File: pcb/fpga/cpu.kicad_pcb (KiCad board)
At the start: 2 copper layers, 0 parts

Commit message: Latest pcb
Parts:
- added C1: 10uF, Capacitors_SMD:C_0805_HandSoldering, F.Cu at (212.1, 82.5)
- added C10: 0.2uF, Capacitors_SMD:C_0805_HandSoldering, B.Cu at (240.0, 83.8)
- added C11: 0.2uF, Capacitors_SMD:C_0805_HandSoldering, B.Cu at (240.0, 88.9)
- added C12: 0.2uF, Capacitors_SMD:C_0805_HandSoldering, B.Cu at (240.0, 94.0)
- added C13: 0.2uF, Capacitors_SMD:C_0805_HandSoldering, B.Cu at (248.9, 78.7)
- added C14: 0.2uF, Capacitors_SMD:C_0805_HandSoldering, B.Cu at (248.9, 83.8)
- added C15: 0.2uF, Capacitors_SMD:C_0805_HandSoldering, B.Cu at (248.9, 88.9)
- added C16: 0.2uF, Capacitors_SMD:C_0805_HandSoldering, B.Cu at (248.9, 94.0)
- added C17: 0.2uF, Capacitors_SMD:C_0805_HandSoldering, B.Cu at (248.9, 99.1)
- added C18: 0.2uF, Capacitors_SMD:C_0805_HandSoldering, B.Cu at (248.9, 104.1)
- added C19: 10uF, Capacitors_SMD:c_elec_4x5.3, F.Cu at (188.0, 94.0)
- added C2: 100uF, Capacitors_SMD:C_0805_HandSoldering, B.Cu at (240.0, 68.6)
- added C20: 1000uF, Capacitors_SMD:c_elec_4x5.3, F.Cu at (198.1, 94.0)
- added C21: 10uF, Capacitors_SMD:c_elec_4x5.3, F.Cu at (204.5, 88.9)
- added C22: 10uF, Capacitors_SMD:c_elec_4x5.3, F.Cu at (218.4, 80.0)
- added C23: 0.1uF, Capacitors_SMD:C_0805, B.Cu at (228.6, 68.6)
- added C24: 0.001uF, Capacitors_SMD:C_0805, B.Cu at (223.5, 68.6)
- added C25: 10uF, Capacitors_SMD:C_0805, F.Cu at (247.7, 81.3)
- added C3: 0.01uF, Capacitors_SMD:C_0805_HandSoldering, B.Cu at (240.0, 73.7)
- added C4: 100uF, Capacitors_SMD:C_0805_HandSoldering, B.Cu at (248.9, 68.6)
- added C5: 0.01uF, Capacitors_SMD:C_0805_HandSoldering, B.Cu at (248.9, 73.7)
- added C6: 10uF, Capacitors_SMD:c_elec_4x4.5, F.Cu at (188.0, 73.7)
- added C7: 1000uF, Capacitors_SMD:c_elec_4x4.5, F.Cu at (198.1, 73.7)
- added C8: 10uF, Capacitors_SMD:c_elec_4x4.5, F.Cu at (204.5, 80.0)
- added C9: 0.2uF, Capacitors_SMD:C_0805_HandSoldering, B.Cu at (240.0, 78.7)
- added CON1: USB-MINI-B, Connect:USB_Mini-B, F.Cu at (188.0, 83.8)
- added D1: LED, LEDs:LED-0805, F.Cu at (222.9, 59.1)
- added D2: LED, LEDs:LED-0805, F.Cu at (219.1, 59.1)
- added D3: LED, LEDs:LED-0805, F.Cu at (215.3, 59.1)
- added D4: LED, LEDs:LED-0805, F.Cu at (211.5, 59.1)
- added D5: LED, LEDs:LED-0805, F.Cu at (207.6, 59.1)
- added D6: LED, LEDs:LED-0805, F.Cu at (203.8, 59.1)
- added D7: LED, LEDs:LED-0805, F.Cu at (200.0, 59.1)
- added D8: LED, LEDs:LED-0805, F.Cu at (196.2, 59.1)
- added FB1: FILTER, Resistors_SMD:R_0805_HandSoldering, F.Cu at (198.1, 83.8)
- added FB2: FILTER, Resistors_SMD:R_0805_HandSoldering, B.Cu at (233.7, 68.6)
- added OSC1: Si501AAA, common-ICs:DFN4-Si501, F.Cu at (223.5, 88.9)
- added P1: PWR, Pin_Headers:Pin_Header_Straight_1x02, F.Cu at (256.5, 101.6)
- added P2: BANK3, Pin_Headers:Pin_Header_Straight_2x08, F.Cu at (254.0, 58.4)
- added P3: BANK1, Pin_Headers:Pin_Header_Straight_2x06, F.Cu at (205.7, 104.1)
- added P4: BANK2, Pin_Headers:Pin_Header_Straight_2x09, F.Cu at (248.9, 58.4)
- added P5: BANK4, Pin_Headers:Pin_Header_Straight_2x09, F.Cu at (243.8, 101.6)
- added P6: CONN_6, Pin_Headers:Pin_Header_Straight_1x06, F.Cu at (256.5, 82.5)
- added R1: 10M, Resistors_SMD:R_0805_HandSoldering, F.Cu at (247.7, 88.9)
- added R2: 24.9, Resistors_SMD:R_0805_HandSoldering, F.Cu at (224.8, 81.3)
- added RP1: 10K, Resistors_SMD:R_Array_Convex_4x1206, F.Cu at (215.9, 95.2)
- added RP2: 270, Housings_DIP:DIP-16_W7.62mm, F.Cu at (222.2, 64.8)
- added U1: EPCS1, SMD_Packages:SOIC-8-N, F.Cu at (213.4, 87.6)
- added U2: LMS1585/7, SMD_Packages:TO-263, B.Cu at (193.0, 76.2)
- added U3: LM1084IS-3.3/NOPB, SMD_Packages:TO-263, B.Cu at (193.0, 91.4)
- added U4: EP1C3T100, Housings_QFP:TQFP-100_14x14mm_Pitch0.5mm, F.Cu at (236.2, 81.3)
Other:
- board outline added: 76.2 x 50.8 mm
- net class Default: clearance 0.254 -> 0.1524; trace_width 0.254 -> 0.1524; via_dia 0.889 -> 0.635; via_drill 0.635 -> 0.3302
- rule trace_clearance: 0.254 -> 0.1524
- rule trace_min: 0.254 -> 0.1524
- rule via_min_drill: 0.508 -> 0.3302
- rule via_min_size: 0.889 -> 0.635

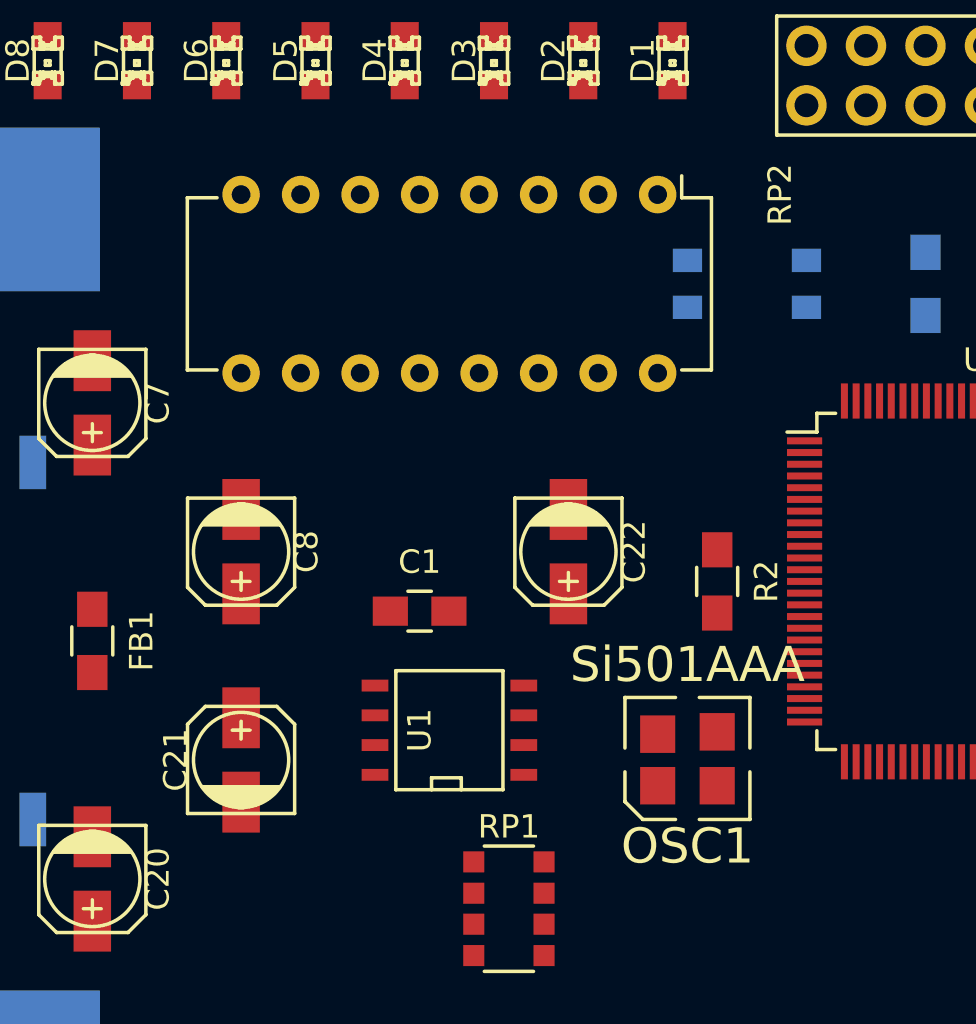
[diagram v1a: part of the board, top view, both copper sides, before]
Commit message: Resistors replacing resistor network
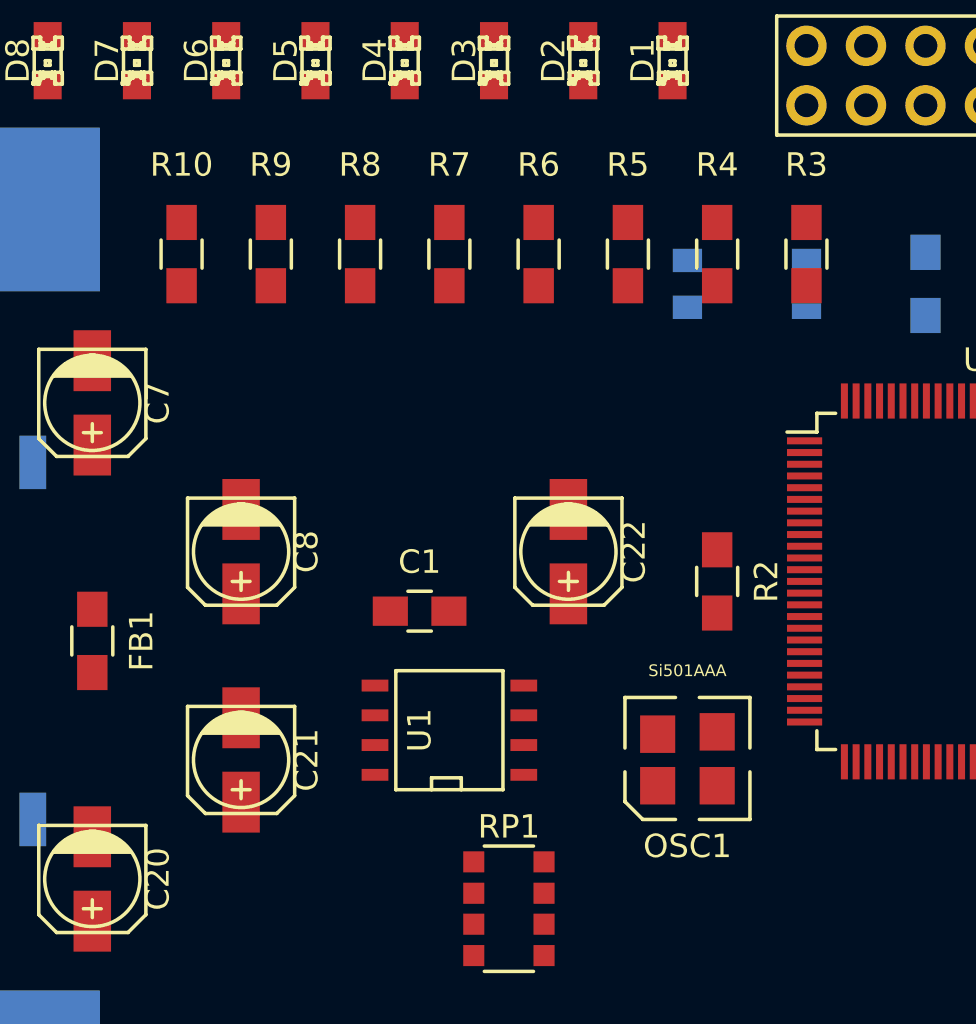
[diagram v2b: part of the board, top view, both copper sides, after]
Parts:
- removed RP2: 270, Housings_DIP:DIP-16_W7.62mm
- added R10: 270, Resistors_SMD:R_0805_HandSoldering, F.Cu at (201.9, 67.3)
- added R3: 270, Resistors_SMD:R_0805_HandSoldering, F.Cu at (228.6, 67.3)
- added R4: 270, Resistors_SMD:R_0805_HandSoldering, F.Cu at (224.8, 67.3)
- added R5: 270, Resistors_SMD:R_0805_HandSoldering, F.Cu at (221.0, 67.3)
- added R6: 270, Resistors_SMD:R_0805_HandSoldering, F.Cu at (217.2, 67.3)
- added R7: 270, Resistors_SMD:R_0805_HandSoldering, F.Cu at (213.4, 67.3)
- added R8: 270, Resistors_SMD:R_0805_HandSoldering, F.Cu at (209.6, 67.3)
- added R9: 270, Resistors_SMD:R_0805_HandSoldering, F.Cu at (205.7, 67.3)
- turned C21 to 270 degrees
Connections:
- net +1.5V renamed VCCINT

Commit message: Layout changes
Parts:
- moved P4 20.5 mm to (228.6, 61.0), turned to 90 degrees
- moved P3 13.0 mm to (218.4, 101.6), turned to 270 degrees
- moved C20 1.27 mm to (196.8, 94.0)
- moved C7 1.27 mm to (196.8, 73.7)
- moved C19 1.27 mm to (189.2, 94.0)
- moved C6 1.27 mm to (189.2, 73.7)
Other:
- board text added: "JTAG"

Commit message: Layout changes
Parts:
- moved R4 1.27 mm to (224.8, 68.6)
- moved R10 0.32 mm to (201.9, 67.6)
- moved R6 0.32 mm to (217.2, 67.6)
- moved R7 0.32 mm to (213.4, 67.6)
- moved R8 0.32 mm to (209.6, 67.6)
- moved R9 0.32 mm to (205.7, 67.6)
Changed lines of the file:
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@@
   )
   (module Resistors_SMD:R_0805_HandSoldering (layer F.Cu)
-    (at 224.79 67.31 90)
+    (at 224.79 68.58 90)
     (descr "Resistor SMD 0805, hand soldering")
     (tags "resistor 0805")
@@
   )
   (module Resistors_SMD:R_0805_HandSoldering (layer F.Cu)
-    (at 217.17 67.31 90)
+    (at 217.17 67.63 90)
     (descr "Resistor SMD 0805, hand soldering")
     (tags "resistor 0805")
@@
   )
   (module Resistors_SMD:R_0805_HandSoldering (layer F.Cu)
-    (at 213.36 67.31 90)
+    (at 213.36 67.63 90)
     (descr "Resistor SMD 0805, hand soldering")
     (tags "resistor 0805")
@@
   )
   (module Resistors_SMD:R_0805_HandSoldering (layer F.Cu)
-    (at 209.55 67.31 90)
+    (at 209.55 67.63 90)
     (descr "Resistor SMD 0805, hand soldering")
     (tags "resistor 0805")
@@
   )
   (module Resistors_SMD:R_0805_HandSoldering (layer F.Cu)
-    (at 205.74 67.31 90)
+    (at 205.74 67.63 90)
     (descr "Resistor SMD 0805, hand soldering")
     (tags "resistor 0805")
@@
   )
   (module Resistors_SMD:R_0805_HandSoldering (layer F.Cu)
-    (at 201.93 67.31 90)
+    (at 201.93 67.63 90)
     (descr "Resistor SMD 0805, hand soldering")
     (tags "resistor 0805")

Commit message: Layout changes
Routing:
- net GND: track 0.00 -> 289.4 mm, vias 0 -> 5
- net +3.3V: track 0.00 -> 255.2 mm, vias 0 -> 4
- net VCCINT: track 0.00 -> 114.1 mm, vias 0 -> 5
- net Net-(C19-Pad1): track 0.00 -> 93.2 mm, vias 0 -> 1
- net 2B13: track 0.00 -> 88.3 mm, vias 0 -> 2
- net 2B12: track 0.00 -> 84.1 mm, vias 0 -> 3
- net 2B10: track 0.00 -> 80.8 mm, vias 0 -> 2
- net 2B11: track 0.00 -> 75.2 mm, vias 0 -> 1
- net 0B13: track 0.00 -> 65.2 mm, vias 0 -> 2
- net 0B12: track 0.00 -> 61.9 mm, vias 0 -> 2
- net 0B10: track 0.00 -> 57.7 mm, vias 0 -> 2
- net 0B11: track 0.00 -> 57.4 mm, vias 0 -> 2
- net 2B23: track 0.00 -> 39.9 mm, vias 0 -> 1
- net 2B15: track 0.00 -> 39.5 mm, vias 0 -> 1
- net 2B24: track 0.00 -> 38.3 mm, vias 0 -> 1
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
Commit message: Layout changes
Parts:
- moved R4 1.27 mm to (224.8, 67.3)
- moved R10 0.32 mm to (201.9, 67.3)
- moved R6 0.32 mm to (217.2, 67.3)
- moved R7 0.32 mm to (213.4, 67.3)
- moved R8 0.32 mm to (209.6, 67.3)
- moved R9 0.32 mm to (205.7, 67.3)
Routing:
- net 2B23: track 39.9 -> 20.8 mm
- net Net-(U1-Pad6): track 21.3 -> 38.4 mm, vias 0 -> 2
- net 2B26: track 26.7 -> 43.1 mm, vias 1 -> 0
- net 2B13: track 88.3 -> 74.5 mm
- net VCCINT: track 114.1 -> 101.0 mm, vias 5 -> 4
- net +3.3V: track 255.2 -> 242.2 mm, vias 4 -> 3
- net 2B21: track 33.7 -> 21.4 mm, vias 0 -> 1
- net 1B23: track 27.8 -> 18.3 mm, vias 0 -> 1
- net 2B34: track 35.3 -> 27.5 mm, vias 1 -> 0
- net 2B15: track 39.5 -> 32.7 mm, vias 1 -> 0
- net 2B35: track 23.3 -> 16.6 mm, vias 0 -> 2
- net 2B43: track 16.5 -> 22.9 mm
- net 2B46: track 21.4 -> 27.5 mm, vias 1 -> 0
- net 0B20: track 31.8 -> 25.9 mm, vias 1 -> 2
- net 0B21: track 29.9 -> 24.3 mm
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
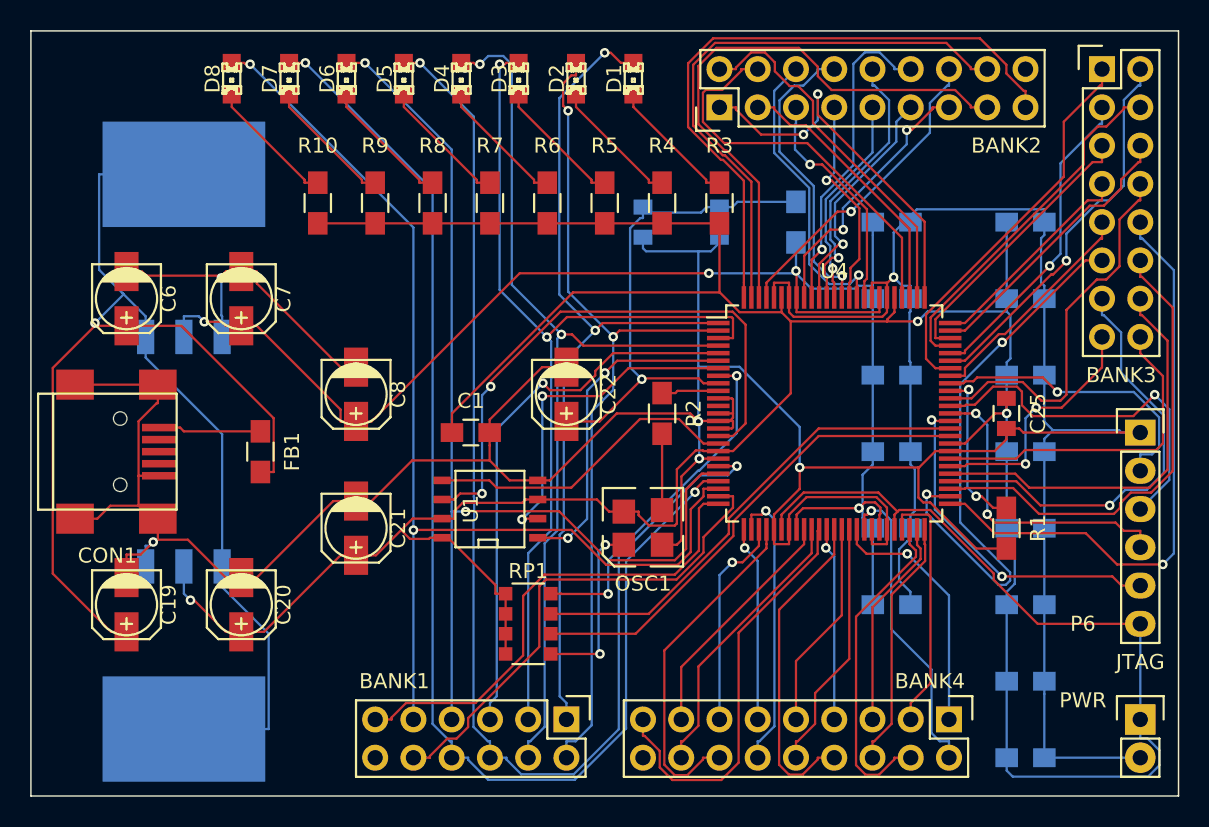
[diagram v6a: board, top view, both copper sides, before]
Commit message: Changed to 8 mil
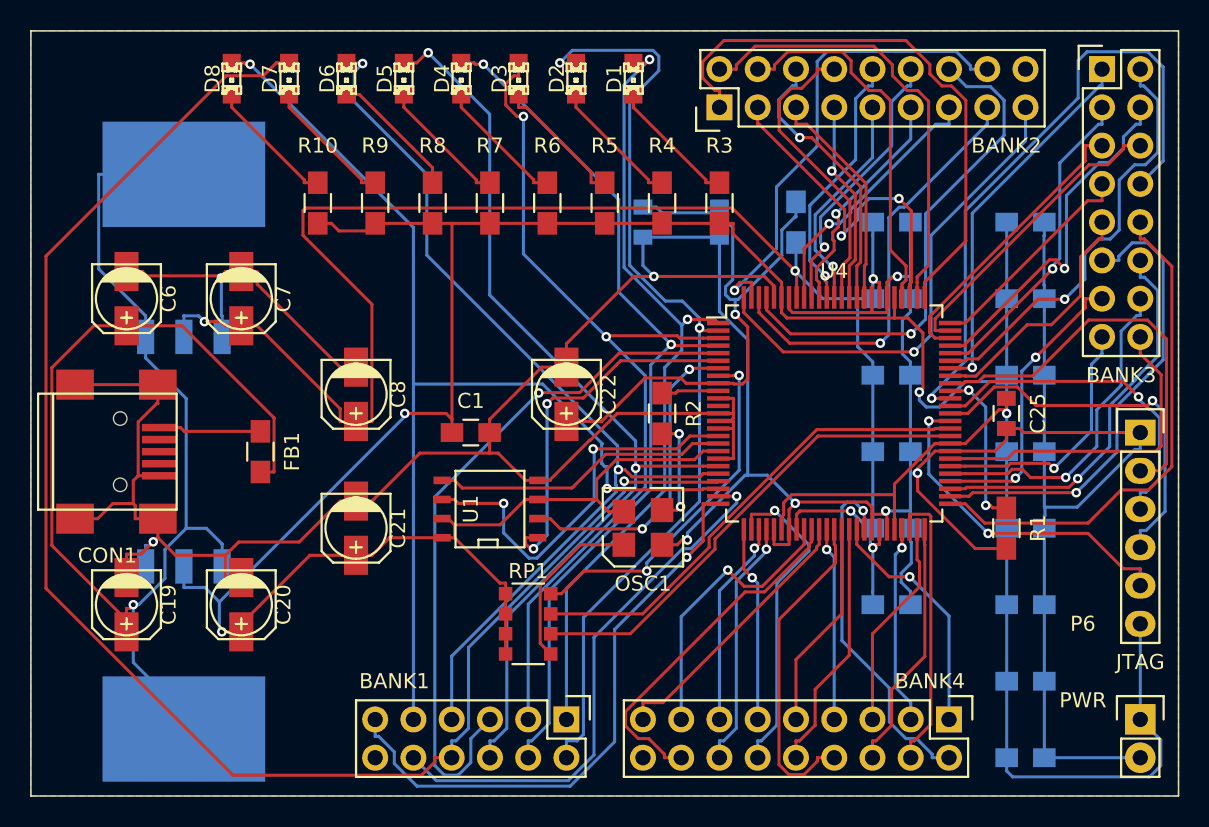
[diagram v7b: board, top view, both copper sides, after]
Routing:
- net 2B12: track 84.5 -> 105.8 mm, vias 2 -> 1
- net 2B10: track 82.6 -> 64.1 mm
- net 1B30: track 25.3 -> 42.4 mm, vias 0 -> 1
- net 2B23: track 20.8 -> 33.7 mm
- net 0B20: track 25.9 -> 37.9 mm, vias 2 -> 0
- net VCCINT: track 101.0 -> 112.8 mm, vias 4 -> 5
- net Net-(U1-Pad6): track 38.4 -> 26.6 mm
- net +3.3V: track 242.2 -> 231.4 mm, vias 3 -> 4
- net 2B26: track 43.1 -> 32.7 mm, vias 0 -> 1
- net 1B10: track 36.8 -> 47.0 mm
- net 2B24: track 38.9 -> 28.7 mm, vias 0 -> 1
- net 2B33: track 29.1 -> 19.4 mm, vias 1 -> 2
- net 2B46: track 27.5 -> 18.2 mm
- net 2B11: track 71.0 -> 63.7 mm
- net TDI: track 19.7 -> 26.8 mm, vias 1 -> 0
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- added copper zone on B.Cu, net GND
- added copper zone on F.Cu, net GND
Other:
- net class Default: trace_width 0.1524 -> 0.2032
